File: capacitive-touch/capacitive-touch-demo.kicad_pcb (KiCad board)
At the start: 2 copper layers, 127.5 x 127.5 mm, 22 parts, among them J1 Conn_01x05_Male, J2 AVR-ISP-6, Q1 BS170, U1 ATmega328P-PU, Y1 16MHz

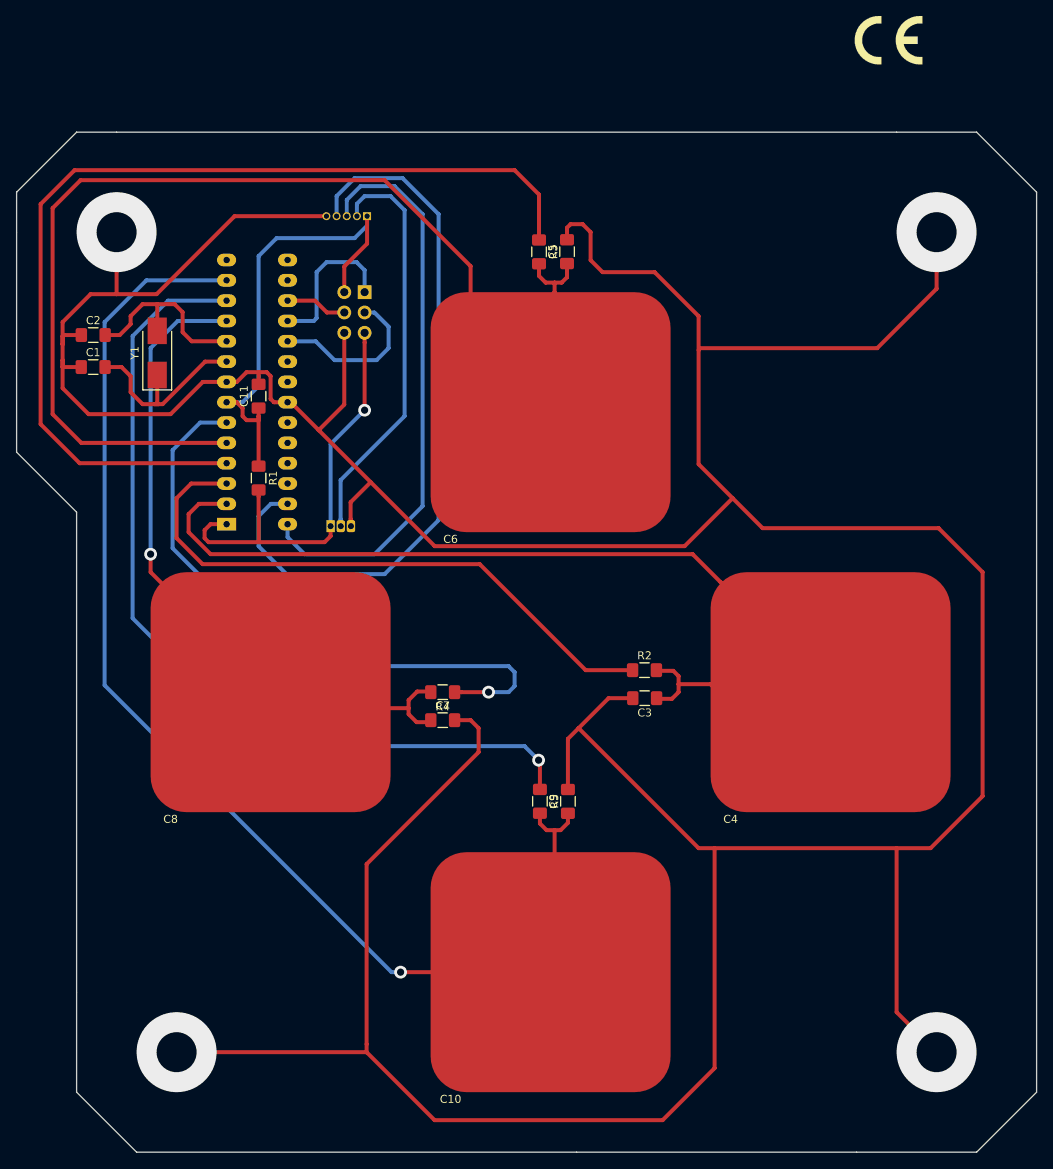
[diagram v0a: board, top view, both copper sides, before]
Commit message: Rerutet og oppdaterte fotavtrykk på pcb til kapacativ touch
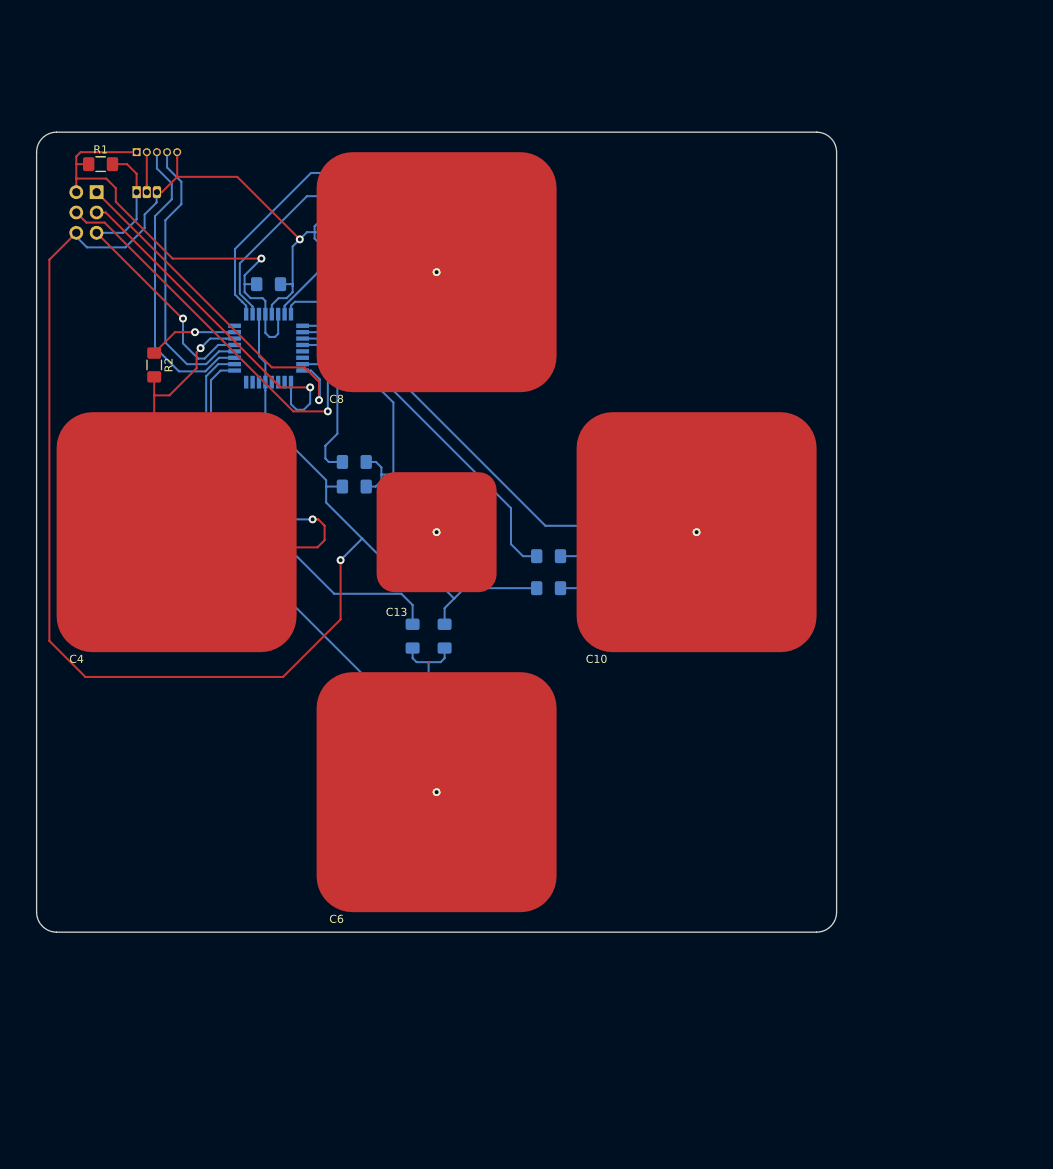
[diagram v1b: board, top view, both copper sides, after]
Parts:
- removed REF**: CE-Logo_8.5x6mm_SilkScreen, Symbol:CE-Logo_8.5x6mm_SilkScreen
- added C12: 100pF, Capacitor_SMD:C_1206_3216Metric_Pad1.42x1.75mm_HandSolder, B.Cu at (119.7, 74.3)
- added C13: capacitive-pad, pads-cap-lib:capacitive-pad-small, F.Cu at (130.0, 80.0)
- added R6: 1M, Resistor_SMD:R_1206_3216Metric_Pad1.42x1.75mm_HandSolder, B.Cu at (119.7, 71.2)
- C1, C11, C2, C3, C5, C7, C9, R3, R4, R5, Y1: moved to B.Cu
- U1: value ATmega328P-PU -> ATmega168-20AU; footprint Package_DIP:DIP-28_W7.62mm_LongPads -> Package_QFP:TQFP-32_7x7mm_P0.8mm
- moved C4 84.2 mm to (97.5, 80.0)
- moved R2 72.2 mm to (94.7, 59.1), turned to 270 degrees
- moved C7 63.8 mm to (117.8, 41.0), turned to 180 degrees
- moved R4 63.4 mm to (117.8, 38.0), turned to 0 degrees
- moved C10 57.9 mm to (162.5, 80.0)
- moved C3 57.3 mm to (107.0, 71.0), turned to 90 degrees
- moved C8 56.5 mm to (130.0, 47.5)
- moved R3 50.6 mm to (127.0, 93.0)
- moved C5 50.4 mm to (131.0, 93.0)
- moved C6 49.6 mm to (130.0, 112.5)
- moved Q1 48.3 mm to (92.5, 37.5)
- moved R1 43.9 mm to (88.0, 34.0), turned to 0 degrees
- moved C2 40.3 mm to (126.8, 48.0), turned to 270 degrees
- moved J2 35.8 mm to (87.5, 37.5)
- moved C1 34.3 mm to (117.8, 44.0)
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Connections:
- J1 pad 3: /SCL -> /SDA
- J1 pad 4: /SDA -> /SCL
- U1 pad 1: /RPin -> Net-(C7-Pad1)
- U1 pad 10: /clk2 -> Net-(R5-Pad1)
- U1 pad 11: Net-(C7-Pad1) -> Net-(C12-Pad1)
- U1 pad 12: Net-(R5-Pad1) -> Net-(R6-Pad1)
- U1 pad 13: Net-(C10-Pad1) -> Net-(U1-Pad13)
- U1 pad 15: Net-(U1-Pad15) -> /MOSI
- U1 pad 16: Net-(U1-Pad16) -> /MISO
- U1 pad 17: /MOSI -> /SCK
- U1 pad 18: /MISO -> Net-(U1-Pad18)
- U1 pad 19: /SCK -> Net-(U1-Pad19)
- U1 pad 2: Net-(C3-Pad1) -> Net-(R4-Pad1)
- U1 pad 21: Net-(U1-Pad21) -> GND
- U1 pad 22: GND -> Net-(U1-Pad22)
- U1 pad 25: Net-(U1-Pad25) -> Net-(R3-Pad1)
- U1 pad 26: Net-(U1-Pad26) -> Net-(C5-Pad1)
- U1 pad 3: Net-(R2-Pad1) -> GND
- U1 pad 4: Net-(R3-Pad1) -> VCC
- U1 pad 5: Net-(C5-Pad1) -> GND
- U1 pad 6: Net-(R4-Pad1) -> VCC
- U1 pad 7: VCC -> /clk1
- U1 pad 8: GND -> /clk2
- U1 pad 9: /clk1 -> Net-(C10-Pad1)
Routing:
- net GND: track 589.4 -> 249.7 mm, vias 4 -> 2
- net Net-(C5-Pad1): track 167.3 -> 81.5 mm, vias 0 -> 1
- net Net-(C10-Pad1): track 158.1 -> 75.3 mm
- net Net-(R3-Pad1): track 123.8 -> 49.3 mm
- net Net-(C3-Pad1): track 142.3 -> 69.2 mm, vias 0 -> 2
- net Net-(R5-Pad1): track 110.7 -> 43.5 mm, vias 1 -> 0
- net Net-(R2-Pad1): track 75.8 -> 11.0 mm, vias 0 -> 1
- net Net-(R4-Pad1): track 79.2 -> 21.4 mm, vias 1 -> 0
- net /SDA: track 91.0 -> 37.9 mm
- net Net-(J1-Pad2): track 51.4 -> 5.00 mm
- net /MOSI: track 7.70 -> 50.4 mm, vias 0 -> 1
- net Net-(C12-Pad1): track 0.00 -> 41.0 mm, vias 0 -> 1
- net /SCL: track 72.0 -> 35.8 mm
- net Net-(C7-Pad1): track 85.4 -> 58.5 mm
- net /MISO: track 19.2 -> 45.2 mm, vias 0 -> 1
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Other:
- board size 127.5 x 127.5 mm -> 100 x 100 mm
- net class Default: clearance 0.1 -> 0.0762; trace_width 0.5 -> 0.254; via_dia 1.6 -> 1; via_drill 0.9 -> 0.5
- rule trace_clearance: 0.1 -> 0.0762
- rule trace_min: 0.3 -> 0.127
- rule via_min_drill: 0.9 -> 0.3
- rule via_min_size: 1.3 -> 0.6
- board text removed: "GND"
- board text removed: "RST"
- board text removed: "SCL"
- board text removed: "SDA"

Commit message: Fikset på kretskort
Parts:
- removed C12, C3, C5, C7, C9: 100pF, Capacitor_SMD:C_1206_3216Metric_Pad1.42x1.75mm_HandSolder
- J1: footprint Connector_PinHeader_1.27mm:PinHeader_1x05_P1.27mm_Vertical -> Connector_PinSocket_2.54mm:PinSocket_1x05_P2.54mm_Vertical_SMD_Pin1Left
- J2: footprint Connector_IDC:IDC-Header_2x03_P2.54mm_Vertical -> Connector_PinSocket_2.54mm:PinSocket_2x03_P2.54mm_Vertical_SMD
- Q1: footprint Package_TO_SOT_THT:TO-92L_Inline -> Package_TO_SOT_SMD:SOT-23_Handsoldering
- R1, R2: moved to B.Cu
- moved J2 40.5 mm to (89.0, 78.0)
- moved R1 39.6 mm to (99.0, 72.0), turned to 90 degrees
- moved Q1 29.8 mm to (97.0, 67.0)
- moved R5 27.9 mm to (146.8, 55.2), turned to 90 degrees
- moved J1 27.9 mm to (88.0, 60.0), turned to 180 degrees
- moved R3 25.9 mm to (110.5, 73.0), turned to 90 degrees
- moved R6 22.8 mm to (140.8, 62.5), turned to 90 degrees
- moved C1 20.2 mm to (137.0, 50.2), turned to 180 degrees
- moved Y1 16.7 mm to (139.0, 46.0), turned to 0 degrees
- moved U1 16.2 mm to (124.0, 63.0)
- moved C11 15.8 mm to (124.5, 52.0), turned to 180 degrees
- moved C2 11.9 mm to (137.0, 54.0), turned to 180 degrees
- moved R2 10.7 mm to (104.0, 64.3), turned to 180 degrees
- moved R4 9.58 mm to (119.0, 47.5), turned to 180 degrees
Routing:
- net GND: track 249.7 -> 23.9 mm, vias 2 -> 6
- net VCC: track 60.1 -> 135.2 mm, vias 1 -> 2
- net /MISO: track 45.2 -> 76.4 mm, vias 1 -> 0
- net Net-(R3-Pad1): track 49.3 -> 20.8 mm
- net /RPin: track 41.2 -> 66.1 mm, vias 1 -> 2
- net Net-(R5-Pad1): track 43.5 -> 22.6 mm
- net Net-(C8-Pad1): track 58.5 -> 40.1 mm
- net /SCK: track 43.5 -> 61.5 mm, vias 1 -> 0
- net Net-(C4-Pad1): track 69.2 -> 54.4 mm
- net Net-(C10-Pad1): track 75.3 -> 60.6 mm
- net Net-(R2-Pad1): track 11.0 -> 25.3 mm, vias 1 -> 2
- net Net-(C6-Pad1): track 81.5 -> 67.4 mm
- net /SCL: track 35.8 -> 46.0 mm
- net Net-(J1-Pad2): track 5.00 -> 13.8 mm
- net /SDA: track 37.9 -> 31.8 mm
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- added copper zone on B.Cu, net GND
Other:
- net class Default: clearance 0.0762 -> 0.127
- rule trace_clearance: 0.0762 -> 0.127

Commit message: Ting fra før sommeren???
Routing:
- net GND: vias 6 -> 9
- net (no net): vias 3 -> 0
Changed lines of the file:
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@@
     (44 Edge.Cuts user)
     (45 Margin user)
-    (46 B.CrtYd user hide)
-    (47 F.CrtYd user hide)
+    (46 B.CrtYd user)
+    (47 F.CrtYd user)
     (48 B.Fab user)
-    (49 F.Fab user hide)
+    (49 F.Fab user)
   )
   (setup
@@
   (gr_arc (start 177.5 32.5) (end 180 32.5) (angle -90) (layer Edge.Cuts) (width 0.15))
   (gr_arc (start 82.5 32.5) (end 82.5 30) (angle -90) (layer Edge.Cuts) (width 0.15))
-  (via (at 85 35) (size 7) (drill 3.5) (layers F.Cu B.Cu) (net 0))
-  (via (at 85 125) (size 7) (drill 3.5) (layers F.Cu B.Cu) (net 0))
-  (via (at 175 125) (size 7) (drill 3.5) (layers F.Cu B.Cu) (net 0))
+  (via (at 85 35) (size 7) (drill 3.5) (layers F.Cu B.Cu) (net 9))
+  (via (at 85 125) (size 7) (drill 3.5) (layers F.Cu B.Cu) (net 9))
+  (via (at 175 125) (size 7) (drill 3.5) (layers F.Cu B.Cu) (net 9))
   (segment (start 146.75 51.65) (end 146.75 53.7625) (width 0.254) (layer B.Cu) (net 1))
   (segment (start 146.8 51.6) (end 146.75 51.65) (width 0.254) (layer B.Cu) (net 1))
